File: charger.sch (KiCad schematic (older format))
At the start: 21 parts, among them IC1 BQ51050B

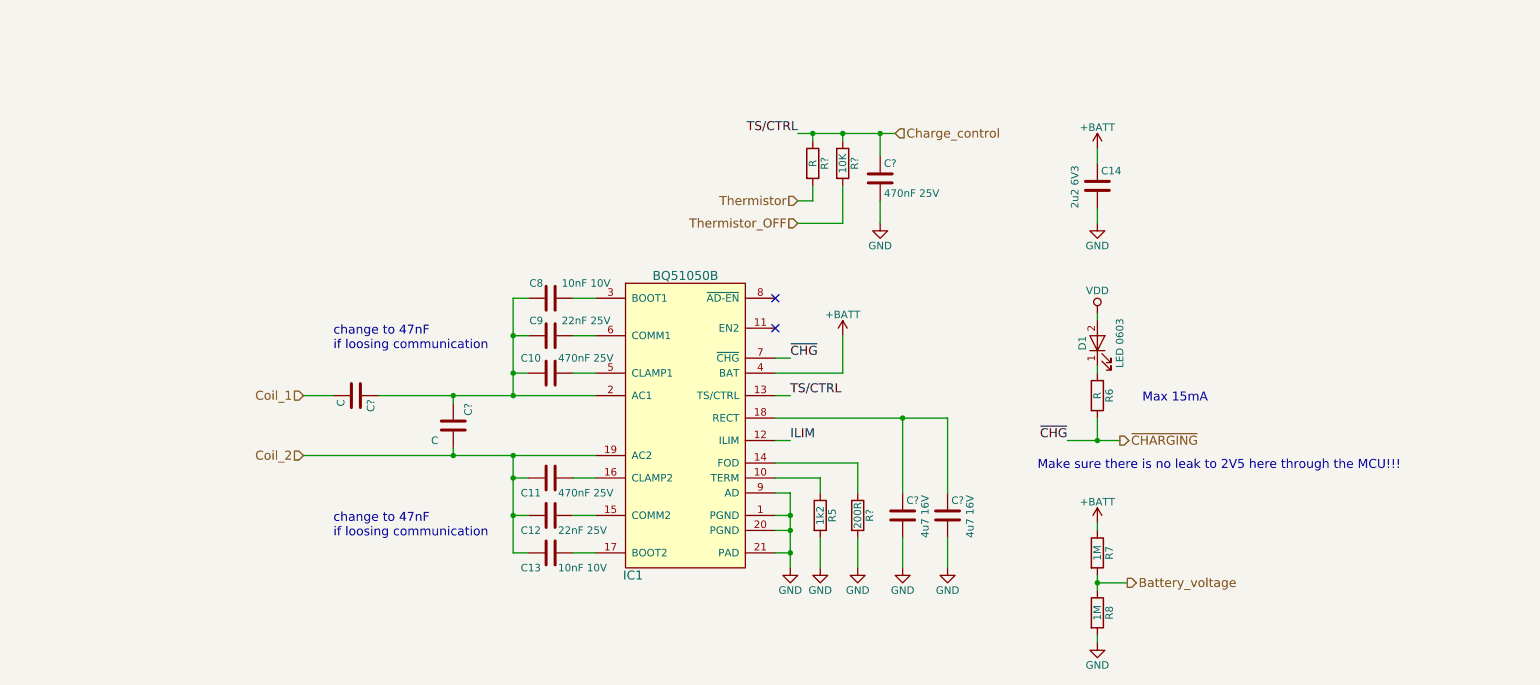
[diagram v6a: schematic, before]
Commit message: Simplified schematic, changed pinout
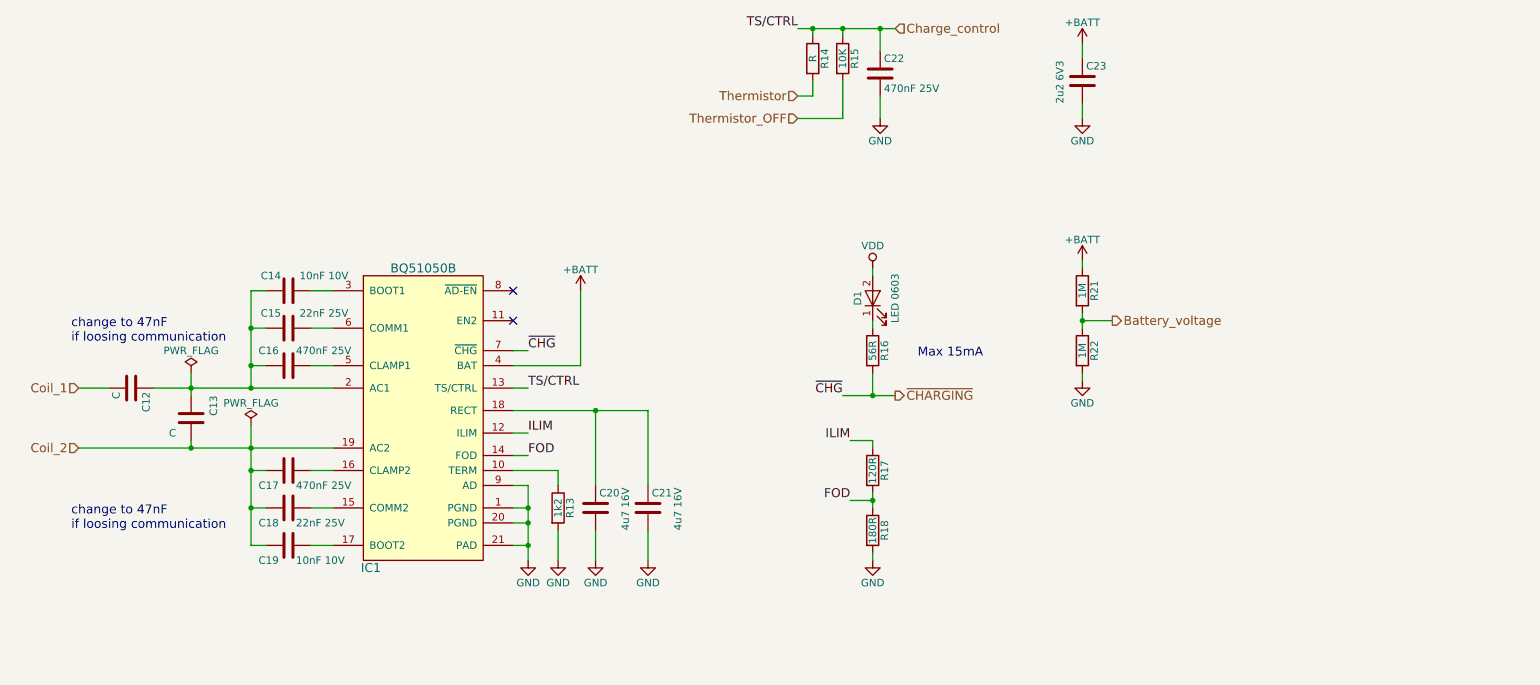
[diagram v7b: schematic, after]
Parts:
- added R17: 120R, Resistors_SMD:R_0402, symbol R
- R13: renamed from R5; footprint (none) -> Resistors_SMD:R_0402
- R14, R15: renamed from R?; footprint (none) -> Resistors_SMD:R_0402
- R16: renamed from R6; value R -> 56R; footprint (none) -> Resistors_SMD:R_0402
- R18: renamed from R?; value 200R -> 180R; footprint (none) -> Resistors_SMD:R_0402
- R21: renamed from R7; footprint (none) -> Resistors_SMD:R_0402
- R22: renamed from R8; footprint (none) -> Resistors_SMD:R_0402
- gave numbers to parts that had none: 5
- renumbered C8 to C14, C9 to C15, C10 to C16, C11 to C17, C12 to C18, C13 to C19, C14 to C23
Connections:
- net ILIM: now also R17.1
- net FOD: now reaches IC1.14 (FOD), R18.1
- net FOD: now also R17.2
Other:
- note removed: "Make sure there is no leak to 2V5 here through the MCU!!!\n"
- moved on the sheet: C12, C13, C14, C15, C16, C17, C18, C19, C20, C21, C22, C23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

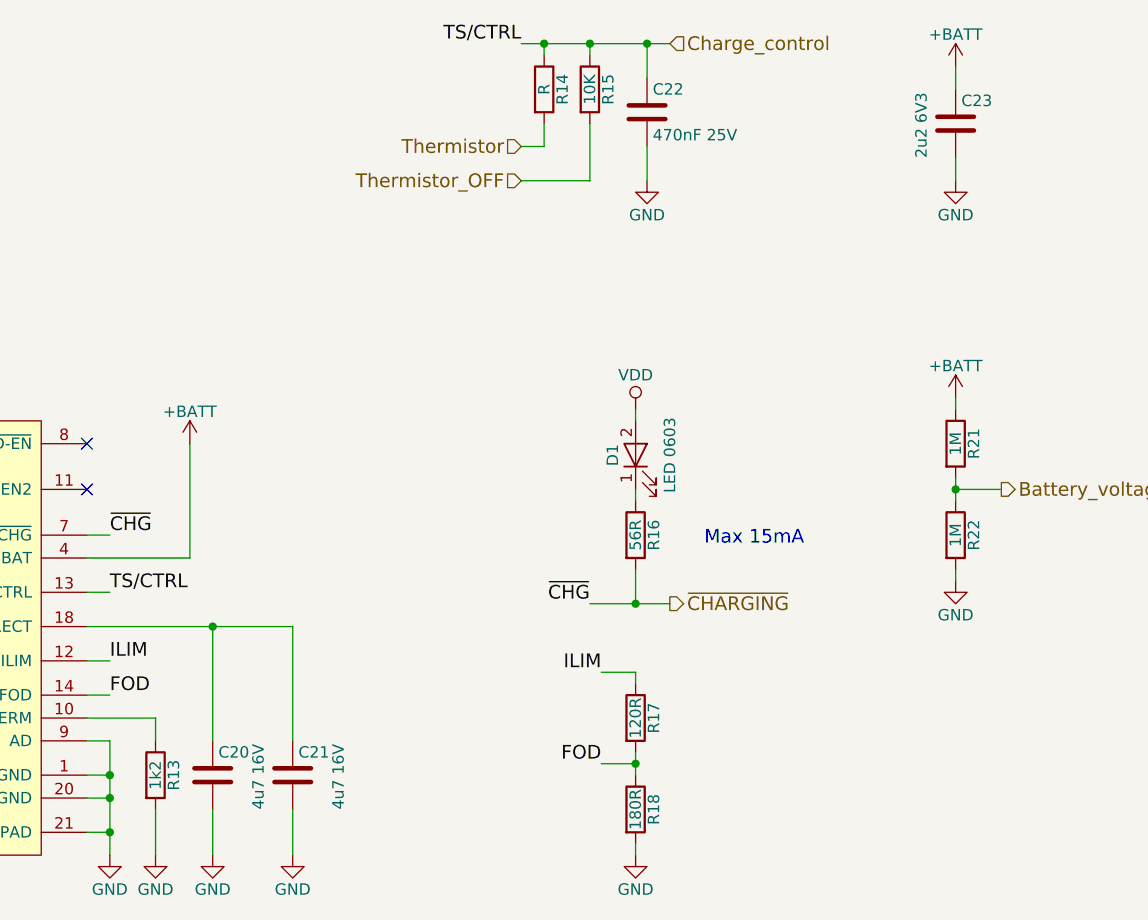
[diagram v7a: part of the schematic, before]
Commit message: Changed pinout, added voltage and current reading
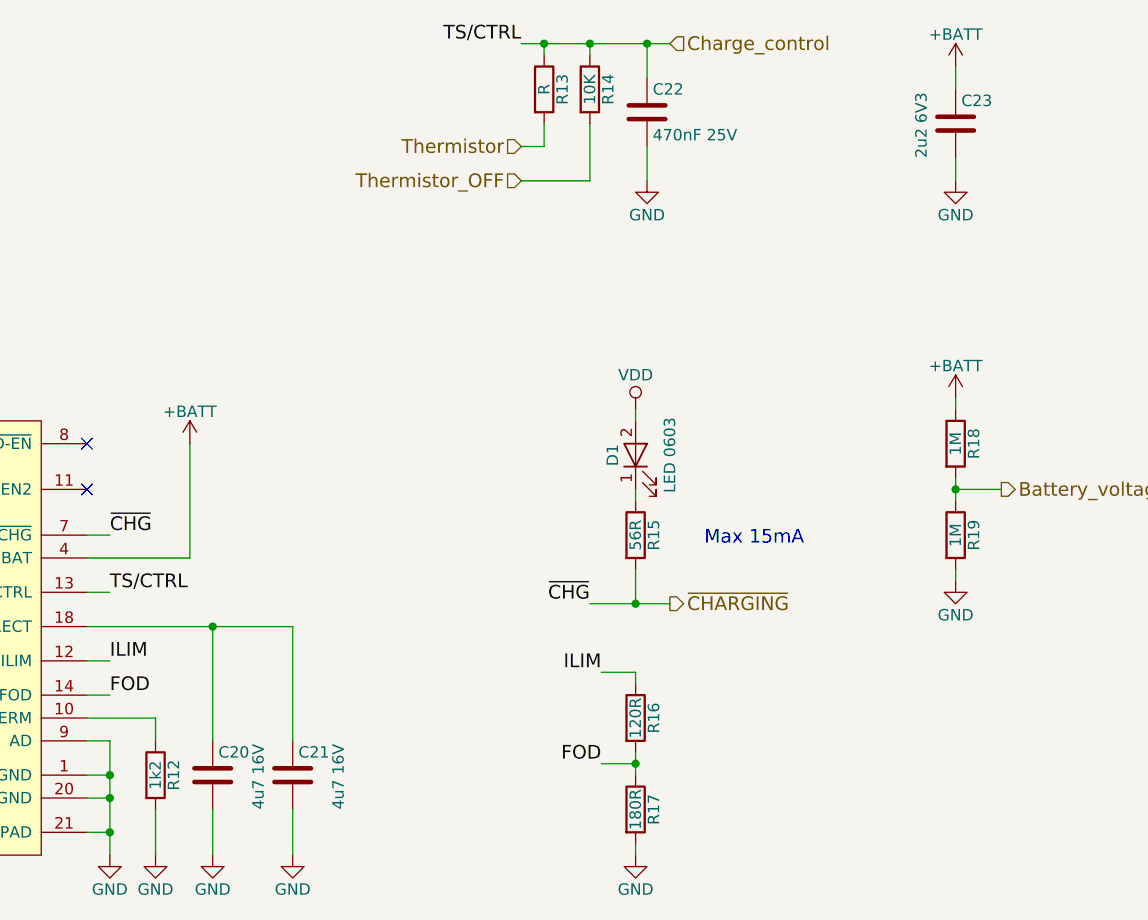
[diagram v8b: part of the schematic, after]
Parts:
- renumbered R13 to R12, R14 to R13, R15 to R14, R16 to R15, R17 to R16, R18 to R17, R21 to R18, R22 to R19
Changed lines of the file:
@@
 Battery_voltage
 $Comp
-L +BATT #PWR038
+L +BATT #PWR50
 U 1 1 5AA78F36
 P 8450 2600
-F 0 "#PWR038" H 8450 2450 50  0001 C CNN
+F 0 "#PWR50" H 8450 2450 50  0001 C CNN
 F 1 "+BATT" H 8450 2740 50  0000 C CNN
 F 2 "" H 8450 2600 50  0001 C CNN
@@
 $EndComp
 $Comp
-L R R21
+L R R18
 U 1 1 5AA78F4C
 P 8450 2800
-F 0 "R21" V 8530 2800 50  0000 C CNN
+F 0 "R18" V 8530 2800 50  0000 C CNN
 F 1 "1M" V 8450 2800 50  0000 C CNN
 F 2 "Resistors_SMD:R_0402" V 8380 2800 50  0001 C CNN
@@
 $EndComp
 $Comp
-L R R22
+L R R19
 U 1 1 5AA78F86
 P 8450 3200
-F 0 "R22" V 8530 3200 50  0000 C CNN
+F 0 "R19" V 8530 3200 50  0000 C CNN
 F 1 "1M" V 8450 3200 50  0000 C CNN
 F 2 "Resistors_SMD:R_0402" V 8380 3200 50  0001 C CNN
@@
 $EndComp
 $Comp
-L GND #PWR039
+L GND #PWR51
 U 1 1 5AA78FC5
 P 8450 3400
-F 0 "#PWR039" H 8450 3150 50  0001 C CNN
+F 0 "#PWR51" H 8450 3150 50  0001 C CNN
 F 1 "GND" H 8450 3250 50  0000 C CNN
 F 2 "" H 8450 3400 50  0001 C CNN
@@
 $EndComp
 $Comp
-L GND #PWR040
+L GND #PWR40
 U 1 1 5AA85C8F
 P 4750 4600
-F 0 "#PWR040" H 4750 4350 50  0001 C CNN
+F 0 "#PWR40" H 4750 4350 50  0001 C CNN
 F 1 "GND" H 4750 4450 50  0000 C CNN
 F 2 "" H 4750 4600 50  0001 C CNN
@@
 $EndComp
 $Comp
-L +BATT #PWR041
+L +BATT #PWR42
 U 1 1 5AA85D44
 P 5100 2800
-F 0 "#PWR041" H 5100 2650 50  0001 C CNN
+F 0 "#PWR42" H 5100 2650 50  0001 C CNN
 F 1 "+BATT" H 5100 2940 50  0000 C CNN
 F 2 "" H 5100 2800 50  0001 C CNN
@@
 NoConn ~ 4650 2800
 $Comp
-L R R16
+L R R15
 U 1 1 5AA85E7B
 P 7050 3200
-F 0 "R16" V 7130 3200 50  0000 C CNN
+F 0 "R15" V 7130 3200 50  0000 C CNN
 F 1 "56R" V 7050 3200 50  0000 C CNN
 F 2 "Resistors_SMD:R_0402" V 6980 3200 50  0001 C CNN
@@
 ~CHARGING
 $Comp
-L R R13
+L R R12
 U 1 1 5AA86C77
 P 4950 4250
-F 0 "R13" V 5030 4250 50  0000 C CNN
+F 0 "R12" V 5030 4250 50  0000 C CNN
 F 1 "1k2" V 4950 4250 50  0000 C CNN
 F 2 "Resistors_SMD:R_0402" V 4880 4250 50  0001 C CNN
@@
 $EndComp
 $Comp
-L GND #PWR042
+L GND #PWR41
 U 1 1 5AA86D68
 P 4950 4600
-F 0 "#PWR042" H 4950 4350 50  0001 C CNN
+F 0 "#PWR41" H 4950 4350 50  0001 C CNN
 F 1 "GND" H 4950 4450 50  0000 C CNN
 F 2 "" H 4950 4600 50  0001 C CNN
@@
 $EndComp
 $Comp
-L +BATT #PWR043
+L +BATT #PWR48
 U 1 1 5AA87B72
 P 8450 1150
-F 0 "#PWR043" H 8450 1000 50  0001 C CNN
+F 0 "#PWR48" H 8450 1000 50  0001 C CNN
 F 1 "+BATT" H 8450 1290 50  0000 C CNN
 F 2 "" H 8450 1150 50  0001 C CNN
@@
 $EndComp
 $Comp
-L GND #PWR044
+L GND #PWR49
 U 1 1 5AA87C01
 P 8450 1650
-F 0 "#PWR044" H 8450 1400 50  0001 C CNN
+F 0 "#PWR49" H 8450 1400 50  0001 C CNN
 F 1 "GND" H 8450 1500 50  0000 C CNN
 F 2 "" H 8450 1650 50  0001 C CNN
@@
 Connection ~ 2900 3300
 $Comp
-L VDD #PWR045
+L VDD #PWR45
 U 1 1 5AA8B638
 P 7050 2650
-F 0 "#PWR045" H 7050 2500 50  0001 C CNN
+F 0 "#PWR45" H 7050 2500 50  0001 C CNN
 F 1 "VDD" H 7050 2800 50  0000 C CNN
 F 2 "" H 7050 2650 50  0001 C CNN
@@
 	2900 3700 2900 4500
 $Comp
-L R R18
+L R R17
 U 1 1 5AB0687F
 P 7050 4400
-F 0 "R18" V 7130 4400 50  0000 C CNN
+F 0 "R17" V 7130 4400 50  0000 C CNN
 F 1 "180R" V 7050 4400 50  0000 C CNN
 F 2 "Resistors_SMD:R_0402" V 6980 4400 50  0001 C CNN
@@
 $EndComp
 $Comp
-L GND #PWR046
+L GND #PWR46
 U 1 1 5AB06991
 P 7050 4600
-F 0 "#PWR046" H 7050 4350 50  0001 C CNN
+F 0 "#PWR46" H 7050 4350 50  0001 C CNN
 F 1 "GND" H 7050 4450 50  0000 C CNN
 F 2 "" H 7050 4600 50  0001 C CNN
@@
 	4650 3600 5550 3600
 $Comp
-L GND #PWR047
+L GND #PWR43
 U 1 1 5AB07537
 P 5200 4600
-F 0 "#PWR047" H 5200 4350 50  0001 C CNN
+F 0 "#PWR43" H 5200 4350 50  0001 C CNN
 F 1 "GND" H 5200 4450 50  0000 C CNN
 F 2 "" H 5200 4600 50  0001 C CNN
@@
 Connection ~ 5200 3600
 $Comp
-L GND #PWR048
+L GND #PWR44
 U 1 1 5AB15630
 P 5550 4600
-F 0 "#PWR048" H 5550 4350 50  0001 C CNN
+F 0 "#PWR44" H 5550 4350 50  0001 C CNN
 F 1 "GND" H 5550 4450 50  0000 C CNN
 F 2 "" H 5550 4600 50  0001 C CNN
@@
 	5550 4400 5550 4600
 $Comp
-L R R14
+L R R13
 U 1 1 5AB15ADC
 P 6650 1250
-F 0 "R14" V 6730 1250 50  0000 C CNN
+F 0 "R13" V 6730 1250 50  0000 C CNN
 F 1 "R" V 6650 1250 50  0000 C CNN
 F 2 "Resistors_SMD:R_0402" V 6580 1250 50  0001 C CNN
@@
 $EndComp
 $Comp
-L GND #PWR049
+L GND #PWR47
 U 1 1 5AB160F7
 P 7100 1650
-F 0 "#PWR049" H 7100 1400 50  0001 C CNN
+F 0 "#PWR47" H 7100 1400 50  0001 C CNN
 F 1 "GND" H 7100 1500 50  0000 C CNN
 F 2 "" H 7100 1650 50  0001 C CNN
@@
 	7100 1500 7100 1650
 $Comp
-L R R15
+L R R14
 U 1 1 5AB17BEE
 P 6850 1250
-F 0 "R15" V 6930 1250 50  0000 C CNN
+F 0 "R14" V 6930 1250 50  0000 C CNN
 F 1 "10K" V 6850 1250 50  0000 C CNN
 F 2 "Resistors_SMD:R_0402" V 6780 1250 50  0001 C CNN
@@
 	7050 4150 7050 4250
 $Comp
-L R R17
+L R R16
 U 1 1 5AB580B7
 P 7050 4000
-F 0 "R17" V 7130 4000 50  0000 C CNN
+F 0 "R16" V 7130 4000 50  0000 C CNN
 F 1 "120R" V 7050 4000 50  0000 C CNN
 F 2 "Resistors_SMD:R_0402" V 6980 4000 50  0001 C CNN
@@
 	7050 3800 7050 3850
 $Comp
-L PWR_FLAG #FLG050
+L PWR_FLAG #FLG1
 U 1 1 5AB77961
 P 2500 3350
-F 0 "#FLG050" H 2500 3425 50  0001 C CNN
+F 0 "#FLG1" H 2500 3425 50  0001 C CNN
 F 1 "PWR_FLAG" H 2500 3500 50  0000 C CNN
 F 2 "" H 2500 3350 50  0001 C CNN
@@
 $EndComp
 $Comp
-L PWR_FLAG #FLG051
+L PWR_FLAG #FLG2
 U 1 1 5AB77A5F
 P 2900 3700
-F 0 "#FLG051" H 2900 3775 50  0001 C CNN
+F 0 "#FLG2" H 2900 3775 50  0001 C CNN
 F 1 "PWR_FLAG" H 2900 3850 50  0000 C CNN
 F 2 "" H 2900 3700 50  0001 C CNN
